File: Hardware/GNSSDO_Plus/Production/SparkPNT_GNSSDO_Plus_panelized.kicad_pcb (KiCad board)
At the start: 4 copper layers, 165.6 x 125.5 mm, 440 parts, among them J1 SMA_Edge, J10 SMA_Edge, J2 USB_C_Receptacle, J3 SMA_Edge, J4 USB_C_Receptacle, J5 MagJack_PoE, J6 microSD, J7 Qwiic_Vertical, J8 SMA_Edge, J9 Screw_Cage_3.5mm-10, Q1 MBT3904DW1, SW1 PTH_RA_h7.5mm, SW2 PTH_RA_h7.5mm, SW3 PTH_RA_h7.5mm, SW4 DPDT_Slide_SMD_7.2x3.5mm, U1 ESP32-WROVER-IE-N16R8, U10 74LVC2T45DC, U11 AP7361C-3.3V, U12 74LVC2T45DC, U13 STP3593LF, U14 74LVC2T45DC, U15 SN74LVC1G175DCK, U16 JPS-3-1+, U17 LMV7219M5, U18 LM66200, U19 PCA9306, U2 mosaic-T, U20 LMV7219M5, U21 LM66200, U22 LM66200, U23 LMV7219M5, U24 LMV7219M5, U25 AP2112K-3.3, U3 CH340C, U4 KSZ8041NL/I, U5 AP7361C-3.3V, U6 REC15E-2405SZ, U7 Ag9205-S, U8 74LVC2T45DC, U9 74LVC2T45DC

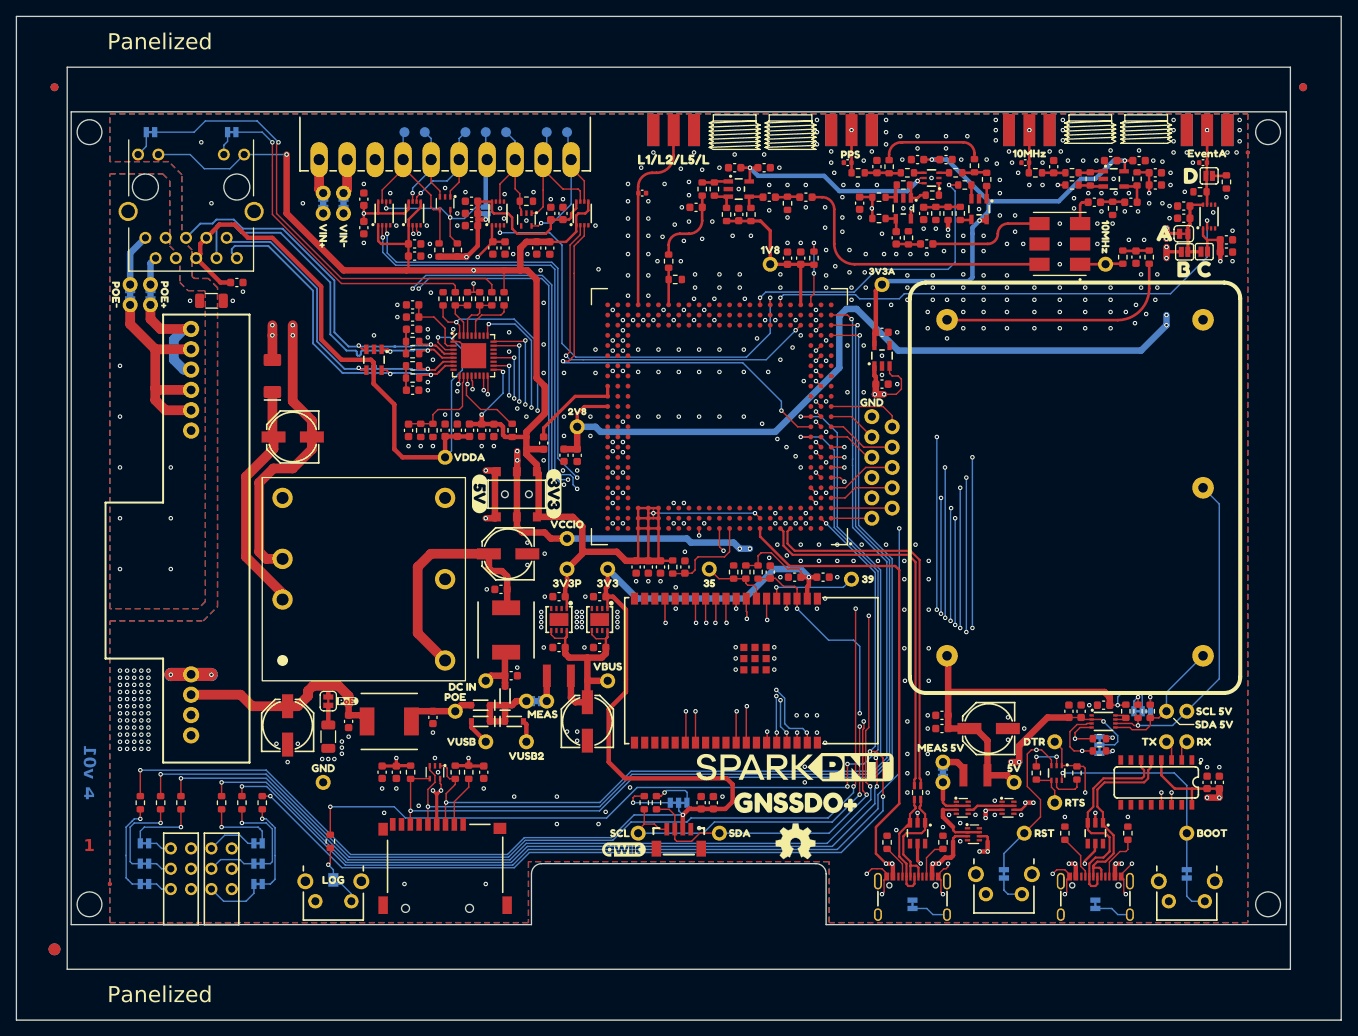
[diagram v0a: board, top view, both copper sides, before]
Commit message: GNSSDO+ v02 PCB - panelized
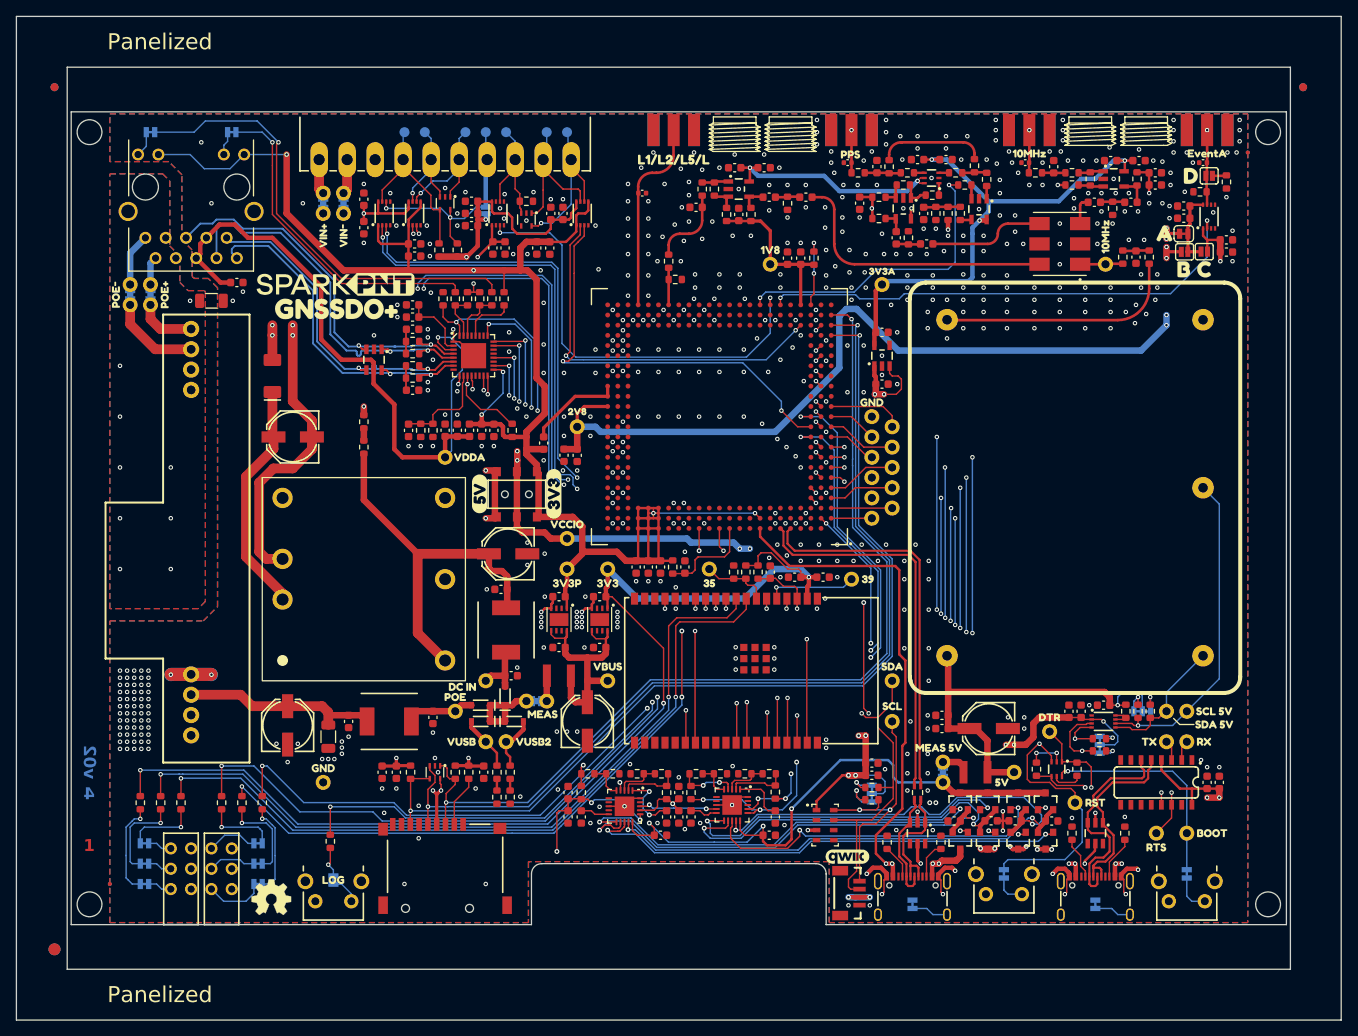
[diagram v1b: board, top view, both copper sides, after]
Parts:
- removed the ? at (99.8, 47.7) (x2)
- removed the ? at (99.8, 155.5) (x2)
- removed the ? at (255.8, 47.7) (x2)
- removed I2C.1, I2C.2, I2C_5V.1: ~, SparkFun-Jumper:Jumper_3_NC-2_Trace
- removed JP1, JP7: ~, SparkFun-Jumper:Jumper_2_NC_Trace
- removed U21, U22: LM66200, SparkFun-Semiconductor-Standard:SOT-583-8
- removed the kibuzzard-65A7F891 at (236.0, 123.2)
- removed kibuzzard-66A212C6: G***, kibuzzard-66A212C6
- removed kibuzzard-66A36AE8 (x2): G***, kibuzzard-66A36AE8
- removed kibuzzard-6780DBA0: G***, kibuzzard-6780DBA0
- added ?: , Fiducial_1mm_Mask3mm, F.Cu at (255.8, 47.7)
- added ?: , Fiducial_1mm_Mask3mm, F.Cu at (99.8, 47.7)
- added ?: , Fiducial_1.5mm_Mask3mm, F.Cu at (99.8, 155.5)
- added ?: , Fiducial_1mm_Mask3mm, B.Cu at (255.8, 47.7)
- added ?: , Fiducial_1mm_Mask3mm, B.Cu at (99.8, 47.7)
- added ?: , Fiducial_1.5mm_Mask3mm, B.Cu at (99.8, 155.5)
- added C100: 4.7uF, SparkFun-Capacitor:C_0603_1608Metric, F.Cu at (164.0, 135.9)
- added C101: 0.1uF, SparkFun-Capacitor:C_0603_1608Metric, F.Cu at (165.6, 138.9)
- added C102: 0.1uF, SparkFun-Capacitor:C_0603_1608Metric, F.Cu at (224.4, 139.4)
- added C103: 10nF, SparkFun-Capacitor:C_0603_1608Metric, F.Cu at (176.3, 138.9)
- added C104: 0.1uF, SparkFun-Capacitor:C_0603_1608Metric, F.Cu at (212.2, 139.4)
- added C105: 0.1uF, SparkFun-Capacitor:C_0603_1608Metric, F.Cu at (189.1, 141.2)
- added C92: 0.1uF, SparkFun-Capacitor:C_0603_1608Metric, F.Cu at (179.3, 138.9)
- added C93: 0.1uF, SparkFun-Capacitor:C_0603_1608Metric, F.Cu at (219.8, 139.4)
- added C94: 10nF, SparkFun-Capacitor:C_0603_1608Metric, F.Cu at (189.9, 138.9)
- added C95: 0.1uF, SparkFun-Capacitor:C_0603_1608Metric, F.Cu at (216.8, 139.4)
- added C96: 0.1uF, SparkFun-Capacitor:C_0603_1608Metric, F.Cu at (175.5, 141.2)
- added C97: 0.1uF, SparkFun-Capacitor:C_0603_1608Metric, F.Cu at (177.8, 138.9)
- added C98: 0.1uF, SparkFun-Capacitor:C_0603_1608Metric, F.Cu at (164.0, 138.9)
- added C99: 4.7uF, SparkFun-Capacitor:C_0603_1608Metric, F.Cu at (177.8, 135.9)
- added JP22: ~, SparkFun-Jumper:Jumper_3_NC-2_Trace, B.Cu at (230.4, 129.9)
- added JP23: ~, SparkFun-Jumper:Jumper_3_NC-2_Trace, B.Cu at (235.7, 125.7)
- added JP24: ~, SparkFun-Jumper:Jumper_3_NC-2_Trace, B.Cu at (201.9, 136.0)
- added JP25: ~, SparkFun-Jumper:Jumper_2_NC_Trace, B.Cu at (134.6, 146.8)
- added Q2: DMG2305UX, SparkFun-Semiconductor-Standard:SOT23-3, F.Cu at (220.2, 141.9)
- added Q3: DMG2305UX, SparkFun-Semiconductor-Standard:SOT23-3, F.Cu at (220.2, 137.0)
- added Q4: DMG2305UX, SparkFun-Semiconductor-Standard:SOT23-3, F.Cu at (216.4, 141.9)
- added Q5: DMG2305UX, SparkFun-Semiconductor-Standard:SOT23-3, F.Cu at (216.4, 137.0)
- added Q6: DMG2305UX, SparkFun-Semiconductor-Standard:SOT23-3, F.Cu at (223.6, 141.9)
- added Q7: DMG2305UX, SparkFun-Semiconductor-Standard:SOT23-3, F.Cu at (223.6, 137.0)
- added Q8: DMG2305UX, SparkFun-Semiconductor-Standard:SOT23-3, F.Cu at (213.0, 141.9)
- added Q9: DMG2305UX, SparkFun-Semiconductor-Standard:SOT23-3, F.Cu at (213.0, 137.0)
- added R46: 200k, SparkFun-Resistor:R_0603_1608Metric, F.Cu at (189.9, 135.8)
- added R49: 47k, SparkFun-Resistor:R_0603_1608Metric, F.Cu at (189.1, 133.5)
- added R80: 47k, SparkFun-Resistor:R_0603_1608Metric, F.Cu at (186.1, 133.5)
- added R81: 200k, SparkFun-Resistor:R_0603_1608Metric, F.Cu at (179.3, 135.9)
- added R82: 47k, SparkFun-Resistor:R_0603_1608Metric, F.Cu at (180.0, 133.5)
- added R83: 47k, SparkFun-Resistor:R_0603_1608Metric, F.Cu at (183.0, 133.5)
- added R84: 200k, SparkFun-Resistor:R_0603_1608Metric, F.Cu at (176.3, 135.9)
- added R85: 47k, SparkFun-Resistor:R_0603_1608Metric, F.Cu at (175.6, 133.5)
- added R86: 47k, SparkFun-Resistor:R_0603_1608Metric, F.Cu at (172.6, 133.5)
- added R87: 200k, SparkFun-Resistor:R_0603_1608Metric, F.Cu at (165.6, 135.9)
- added R88: 47k, SparkFun-Resistor:R_0603_1608Metric, F.Cu at (166.4, 133.5)
- added R89: 47k, SparkFun-Resistor:R_0603_1608Metric, F.Cu at (169.5, 133.5)
- added R92: 100, SparkFun-Resistor:R_0603_1608Metric, F.Cu at (138.4, 92.7)
- added R93: 100, SparkFun-Resistor:R_0603_1608Metric, F.Cu at (138.4, 89.5)
- added R94: 100, SparkFun-Resistor:R_0603_1608Metric, F.Cu at (156.7, 133.3)
- added R95: 100, SparkFun-Resistor:R_0603_1608Metric, F.Cu at (156.7, 136.5)
- added R96: 100, SparkFun-Resistor:R_0603_1608Metric, F.Cu at (155.1, 133.3)
- added R97: 100, SparkFun-Resistor:R_0603_1608Metric, F.Cu at (155.1, 136.5)
- added U26: LTC4418, SparkFun-Semiconductor-Standard:QFN-20-1EP_4x4mm_P0.5mm_EP2.45x2.45mm, F.Cu at (184.5, 137.4)
- added U27: LTC4418, SparkFun-Semiconductor-Standard:QFN-20-1EP_4x4mm_P0.5mm_EP2.45x2.45mm, F.Cu at (171.0, 137.6)
- added kibuzzard-68419E21: G***, kibuzzard-68419E21, B.Cu at (235.7, 123.4)
- added kibuzzard-68419E42: G***, kibuzzard-68419E42, B.Cu at (229.9, 146.4)
- added kibuzzard-68419E53: G***, kibuzzard-68419E53, B.Cu at (207.0, 146.6)
- added kibuzzard-68419EB2: G***, kibuzzard-68419EB2, B.Cu at (153.7, 66.8)
- G***: footprint SparkFun-Aesthetic:SparkPNT_Logo_25mm -> SparkFun-Aesthetic:SparkPNT_Logo_20mm
- J7: footprint SparkFun-Connector:JST_SMD_1.0mm-4_Vertical -> SparkFun-Connector:JST_SMD_1.0mm-4_Vertical_Black
- U11, U5: footprint SparkFun-Semiconductor-Standard:UDFN-8 -> SparkFun-Semiconductor-Standard:DFN-8_3x3mm_P0.65mm_EP2.25x1.5mm
- U18: value LM66200 -> MS8607-02BA; footprint SparkFun-Semiconductor-Standard:SOT-583-8 -> SparkFun-Semiconductor-Standard:LGA-8_3x5mm_P1.25mm
- U7: value Ag9205-S -> DP5305; footprint SparkFun-Semiconductor-Nonstandard:Ag9200 -> SparkFun-Semiconductor-Nonstandard:DP5300
- moved kibuzzard-677FF212 84.3 mm to (135.0, 75.4)
- moved G*** 83.3 mm to (135.0, 72.4)
- moved Ref** 65.9 mm to (126.9, 149.2)
- moved kibuzzard-66A12184 37.6 mm to (204.5, 125.1) (x2)
- moved TP25 34.7 mm to (204.5, 127.0)
- moved TP26 28.8 mm to (204.5, 121.9)
- moved R6 28.5 mm to (201.9, 136.8), turned to 0 degrees
- moved kibuzzard-66A12197 28.2 mm to (204.5, 120.1) (x2)
- moved G*** 28.0 mm to (198.9, 143.9)
- moved R4 27.0 mm to (201.9, 135.3), turned to 0 degrees
- moved kibuzzard-65A7F891 23.5 mm to (204.5, 136.0)
- moved J7 22.1 mm to (198.9, 148.5), turned to 90 degrees
- moved C54 21.6 mm to (201.9, 133.7), turned to 0 degrees
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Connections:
- C36 pad 1: Net-(JP7-B) -> Net-(U7-VOUT+)
- C37 pad 1: Net-(JP7-B) -> Net-(U7-VOUT+)
- J6 pad 11: (no net) -> unconnected-(J6-SHIELD-Pad11)
- J6 pad 12: (no net) -> unconnected-(J6-SHIELD-Pad12)
- J6 pad 13: (no net) -> unconnected-(J6-SHIELD-Pad13)
- JP14 pad 1: Net-(JP14-A) -> VOCXO
- JP4 pad 2: VIN+ -> Net-(JP4-B)
- JP5 pad 2: VIN- -> Net-(JP5-B)
- L4 pad 1: Net-(JP7-B) -> Net-(U7-VOUT+)
- R36 pad 1: Net-(JP7-A) -> Net-(U7-VOUT+)
- U18 pad 1: GND -> 3.3V
- U18 pad 2: Net-(U22-VIN1) -> unconnected-(U18-NC-Pad2)
- U18 pad 3: VUSB -> GND
- U18 pad 4: GND -> unconnected-(U18-NC-Pad4)
- U18 pad 5: GND -> unconnected-(U18-NC-Pad5)
- U18 pad 6: VUSB2 -> unconnected-(U18-NC-Pad6)
- U18 pad 7: Net-(U22-VIN1) -> ESP21/SDA
- U18 pad 8: unconnected-(U18-ST-Pad8) -> ESP22/SCL
- U7 pad 1: VIN+ -> Net-(JP4-B)
- U7 pad 2: VIN- -> Net-(JP5-B)
- U7 pad 3: VIN+ -> unconnected-(U7-ATD-Pad3)
- U7 pad 4: VIN- -> unconnected-(U7-NC-Pad4)
- U7 pad 5: VIN- -> GND
- U7 pad 6: unconnected-(U7-CP-Pad6) -> Net-(U7-VOUT+)
- U7 pad 7: GND -> unconnected-(U7-ADJ-Pad7)
- U7 pad 8: Net-(JP7-B) -> GND
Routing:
- net VOCXO: track 0.00 -> 72.9 mm, vias 0 -> 3
- net G3: track 0.00 -> 65.5 mm, vias 0 -> 3
- net VS3: track 0.00 -> 59.4 mm, vias 0 -> 2
- net VS4: track 0.00 -> 58.8 mm, vias 0 -> 2
- net LED_PVT: track 150.1 -> 91.5 mm, vias 3 -> 4
- net G4: track 0.00 -> 55.5 mm, vias 0 -> 3
- net VS1: track 0.00 -> 50.2 mm, vias 0 -> 2
- net G1: track 0.00 -> 48.5 mm, vias 0 -> 3
- net VS2: track 0.00 -> 47.4 mm, vias 0 -> 2
- net G2: track 0.00 -> 45.7 mm, vias 0 -> 3
- net ESP32/LED_ERROR: track 137.2 -> 94.3 mm, vias 4 -> 2
- net ESP33/LED_LOCK: track 136.7 -> 96.2 mm, vias 4 -> 2
- net Net-(JP7-B): track 28.6 -> 0.00 mm
- net VUSB: track 138.6 -> 166.4 mm, vias 5 -> 8
- net VIN-: track 27.3 -> 0.00 mm
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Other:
- board text added: "Material: TG135"
- board text added: "v02"
- board text removed: "Material: TG155"
- board text removed: "P.C."
- board text removed: "v01"
